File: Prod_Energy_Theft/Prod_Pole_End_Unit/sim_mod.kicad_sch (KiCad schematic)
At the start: 23 parts, among them J23 U.FL-R-SMT_01_, J28 JAE_SIM_Card_SF72S006, Q2 2N3904, U17 TXS0108EPW, U18 SIM7600G, U20 USBLC6-2SC6, U21 USBLC6-2SC6

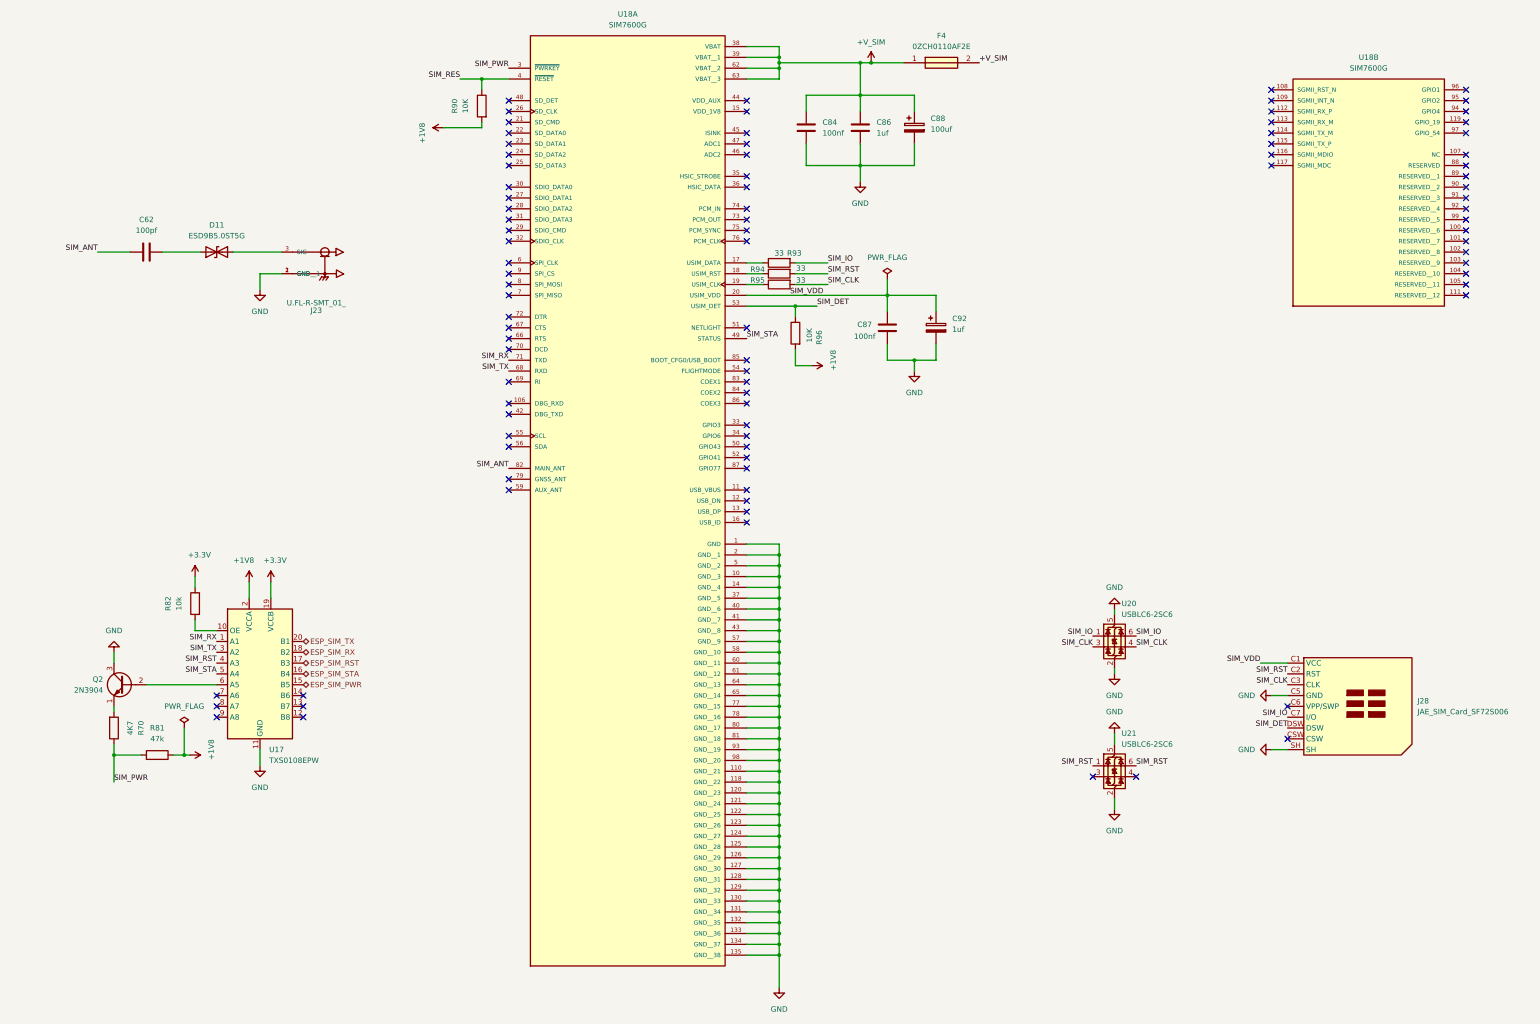
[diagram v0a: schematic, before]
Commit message: Chnages in power and ADE7816
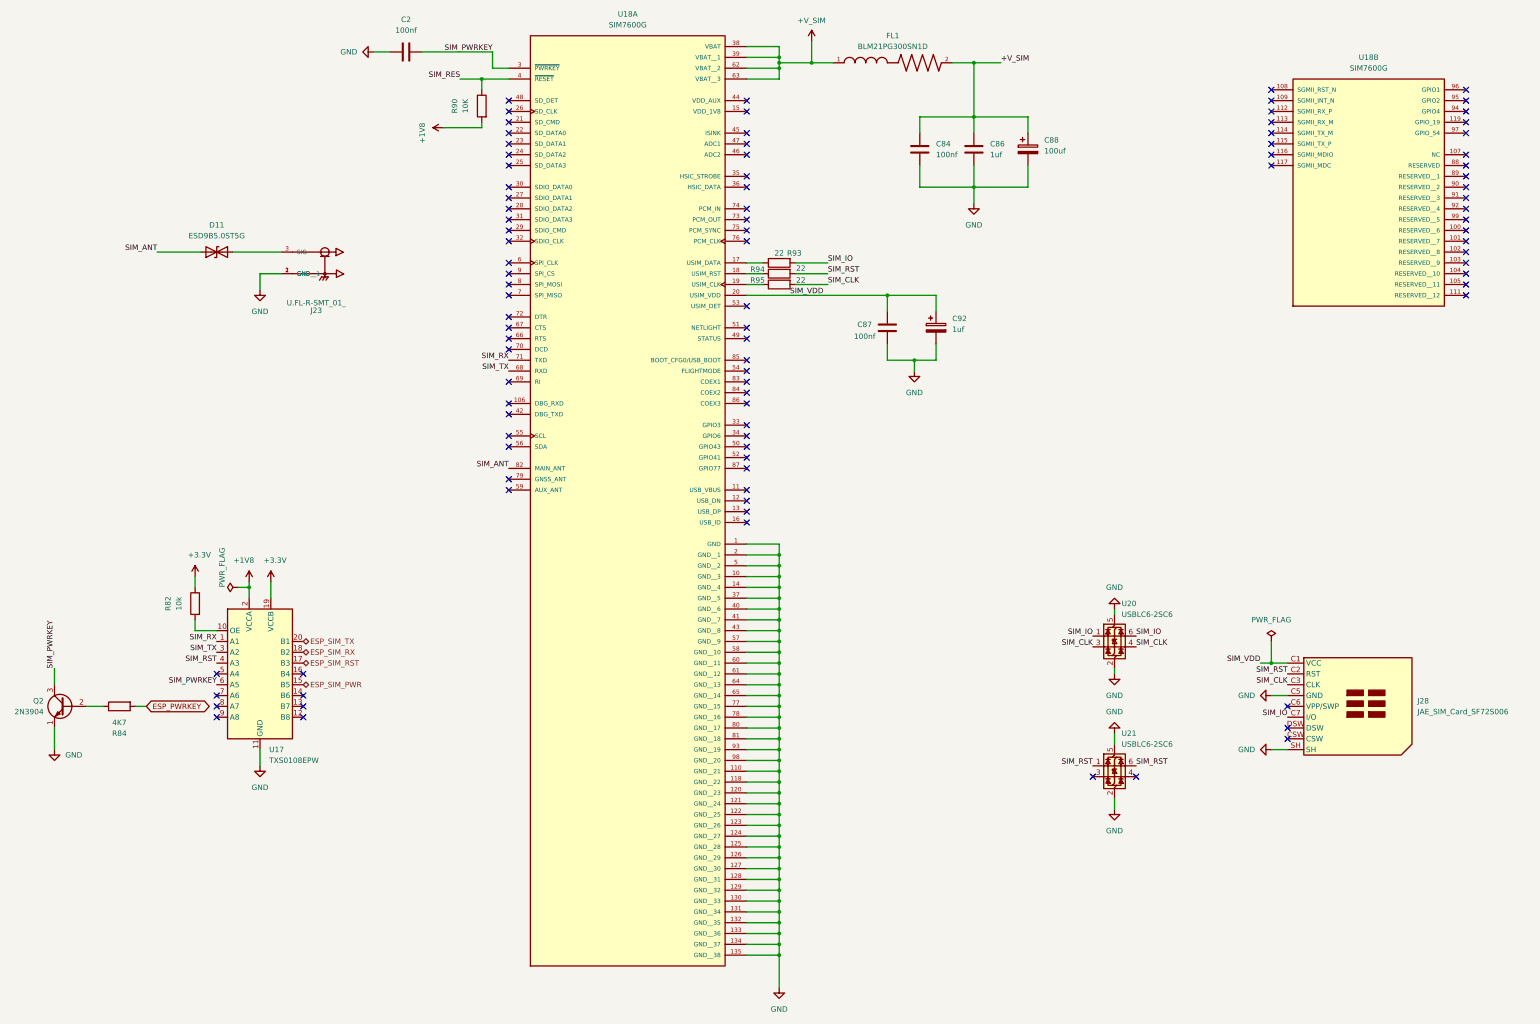
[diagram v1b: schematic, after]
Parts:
- removed C62: 100pf, Capacitor_SMD:C_0805_2012Metric, symbol Device:C
- removed F4: 0ZCH0110AF2E, Footprints.kicad_mod:FUSC3226X100N, symbol 0ZCH0110AF2E:0ZCH0110AF2E
- removed R70: 4K7, Resistor_SMD:R_0805_2012Metric, symbol Device:R
- removed R81: 47k, Resistor_SMD:R_0805_2012Metric, symbol Device:R
- removed R96: 10K, Resistor_SMD:R_0805_2012Metric, symbol Device:R
- added C2: 100nf, symbol Device:C
- added FL1: BLM21PG300SN1D, BLM21PG300SN1D:BEADC2012X105N, symbol BLM21PG300SN1D:BLM21PG300SN1D
- added R84: 4K7, Resistor_SMD:R_0805_2012Metric, symbol Device:R
- R93, R94, R95: value 33 -> 22
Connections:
- net +V_SIM: now also FL1.1, FL1.2
- net GND: now also Q2.1 (E), C2.1; no longer Q2.3 (C)
- net SIM_ANT: now also D11.1 (A1)
- net at Q2.2 (B): now also R84.1; no longer U17.6 (A5)
- net ESP_SIM_STA: no longer names the net of U17.16 (B4)
- net SIM_DET: no longer names the net of U18.53 (USIM_DET)
- net SIM_DET: no longer J28.DSW
- net SIM_PWR renamed SIM_PWRKEY
- net SIM_PWRKEY: now also Q2.3 (C), U17.6 (A5), C2.2
- net SIM_STA: no longer names the net of U17.5 (A4)
- net SIM_STA: no longer U18.49 (STATUS)
- new net ESP_PWRKEY: R84.2
- no-connect marks 91 -> 96
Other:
- moved on the sheet: C84, C86, C88, Q2

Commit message: PCB
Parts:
- C2: footprint (none) -> Capacitor_SMD:C_0805_2012Metric
- FL1: footprint BLM21PG300SN1D:BEADC2012X105N -> theftdetection:BEADC2012X105N
- J23: footprint U.FL-R-SMT_01_:HRS_U.FL-R-SMT_01_ -> theftdetection:HRS_U.FL-R-SMT_01_
- U18: footprint SIM7600G:IC_SIM7600G -> theftdetection:IC_SIM7600G
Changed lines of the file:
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@@
 	(wire
 		(pts
-			(xy 204.47 95.25) (xy 237.49 95.25)
-		)
-		(stroke
-			(width 0)
-			(type default)
-		)
-	)
-	(wire
-		(pts
 			(xy 212.09 194.31) (xy 212.09 196.85)
 		)
@@
 	(wire
 		(pts
+			(xy 204.47 95.25) (xy 237.49 95.25)
+		)
+		(stroke
+			(width 0)
+			(type default)
+		)
+	)
+	(wire
+		(pts
 			(xy 290.83 168.91) (xy 290.83 170.18)
 		)
@@
 			)
 		)
-		(property "Footprint" "SIM7600G:IC_SIM7600G"
+		(property "Footprint" "theftdetection:IC_SIM7600G"
 			(at 176.53 90.17 0)
 			(effects
@@
 			)
 		)
-		(property "Footprint" ""
+		(property "Footprint" "Capacitor_SMD:C_0805_2012Metric"
 			(at 128.27 37.1348 0)
 			(effects
@@
 			)
 		)
-		(property "Footprint" "SIM7600G:IC_SIM7600G"
+		(property "Footprint" "theftdetection:IC_SIM7600G"
 			(at 350.52 57.15 0)
 			(effects
@@
 			)
 		)
-		(property "Footprint" "BLM21PG300SN1D:BEADC2012X105N"
+		(property "Footprint" "theftdetection:BEADC2012X105N"
 			(at 240.03 40.64 0)
 			(effects
@@
 			)
 		)
-		(property "Footprint" "U.FL-R-SMT_01_:HRS_U.FL-R-SMT_01_"
+		(property "Footprint" "theftdetection:HRS_U.FL-R-SMT_01_"
 			(at 105.41 87.63 0)
 			(effects

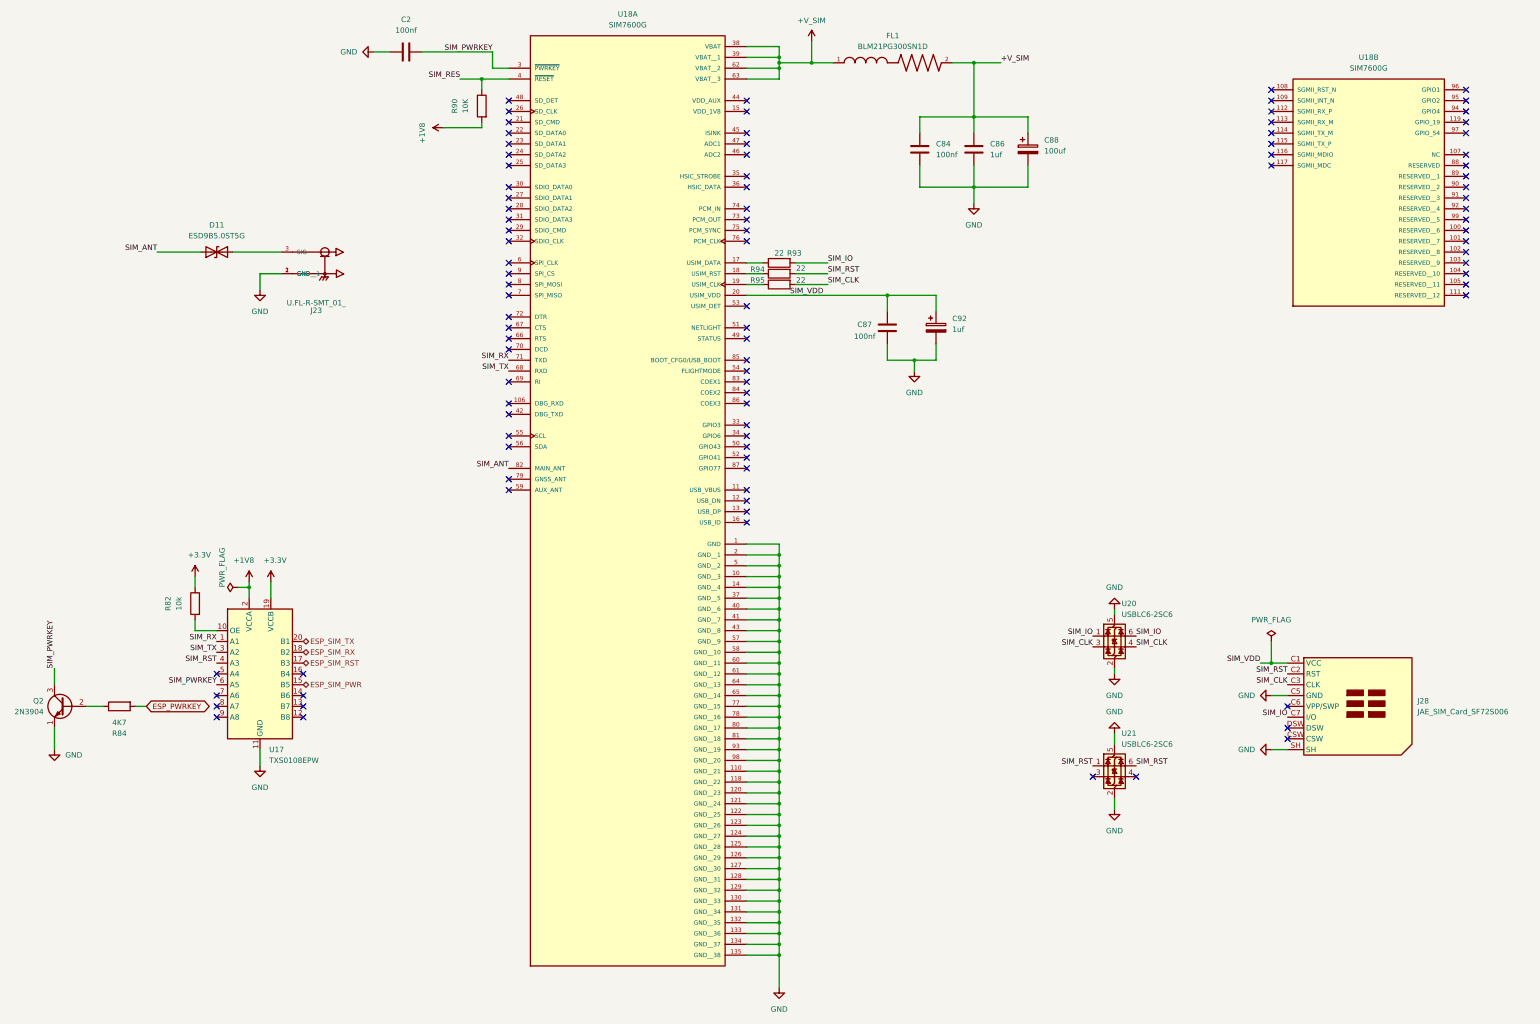
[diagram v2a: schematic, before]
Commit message: update in BOM list
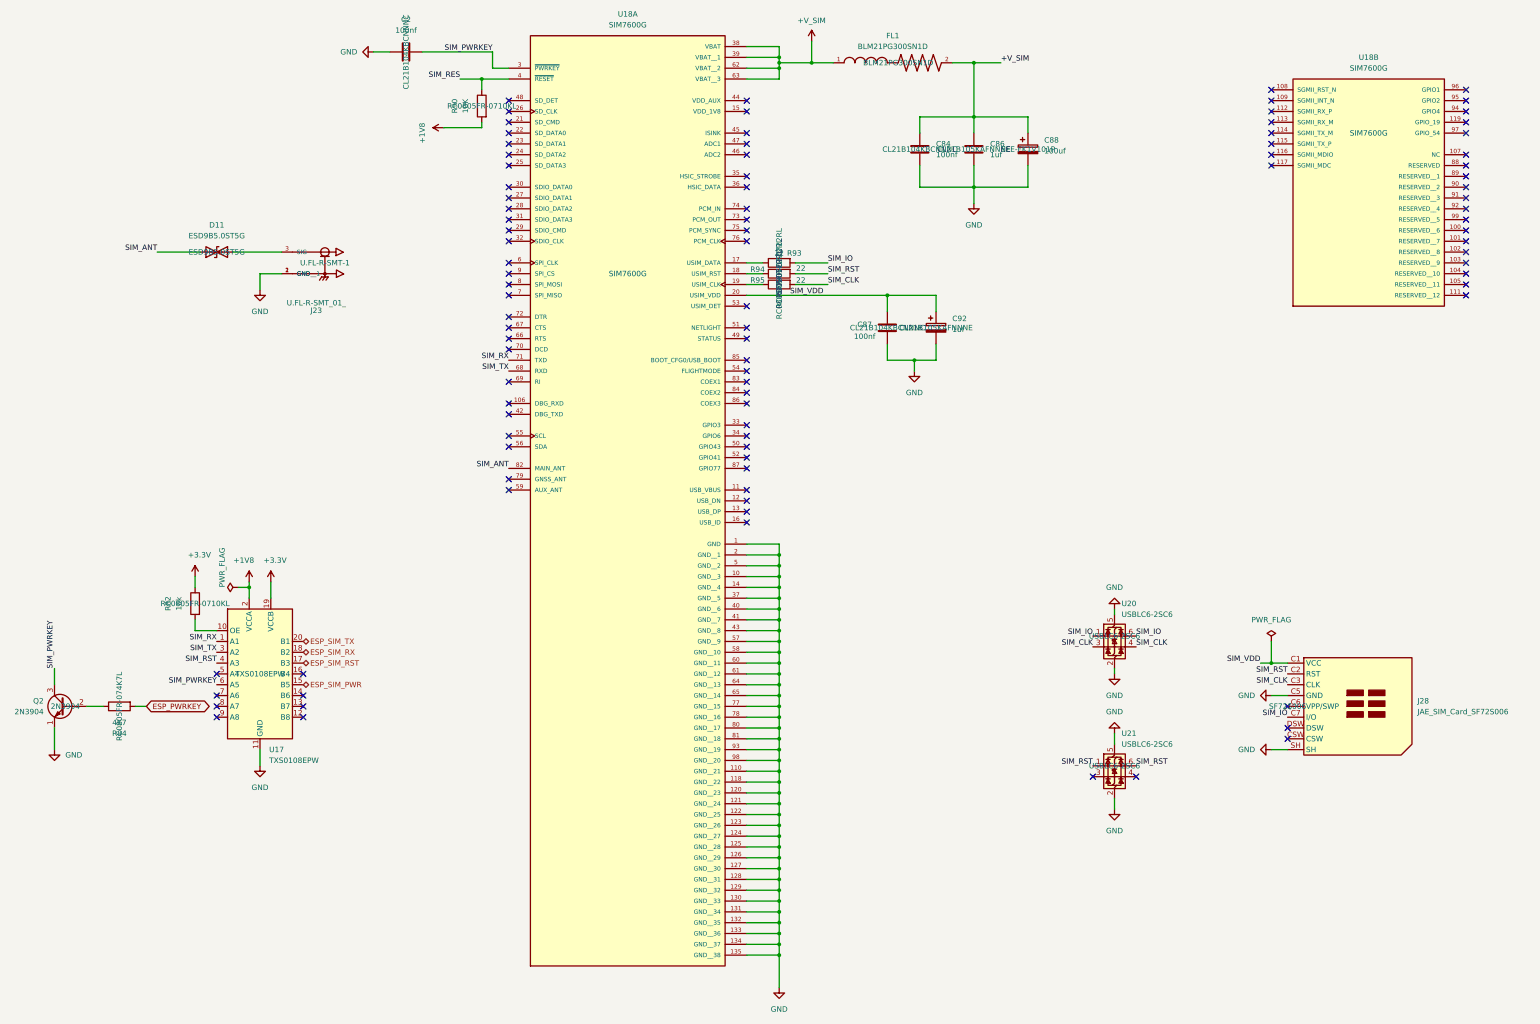
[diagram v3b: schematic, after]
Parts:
- C2, C84, C87: Part Number (none) -> CL21B104KBCNNNC
- C86, C92: Part Number (none) -> CL21B105KAFNNNE
- C88: Part Number (none) -> EEE-FK1V101P
- D11: Part Number (none) -> ESD9B5.0ST5G
- FL1: Part Number (none) -> BLM21PG300SN1D
- J23: Part Number (none) -> U.FL-R-SMT-1
- J28: Part Number (none) -> SF72S006
- Q2: Part Number (none) -> 2N3904
- R82, R90: Part Number (none) -> RC0805FR-0710KL
- R84: Part Number (none) -> RC0805FR-074K7L
- R93, R94, R95: Part Number (none) -> RC0805FR-0722RL
- U17: Part Number (none) -> TXS0108EPW
- U18: Part Number (none) -> SIM7600G
- U20, U21: Part Number (none) -> USBLC6-2SC6
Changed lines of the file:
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@@
 			)
 		)
+		(property "Part Number" "RC0805FR-0722RL "
+			(at 212.09 90.17 0)
+			(effects
+				(font
+					(size 1.27 1.27)
+				)
+			)
+		)
 		(pin "1"
 		)
@@
 			)
 		)
+		(property "Part Number" "RC0805FR-0710KL "
+			(at 74.93 167.64 0)
+			(effects
+				(font
+					(size 1.27 1.27)
+				)
+			)
+		)
 		(pin "1"
 		)
@@
 			)
 		)
+		(property "Part Number" "TXS0108EPW "
+			(at 90.17 184.15 0)
+			(effects
+				(font
+					(size 1.27 1.27)
+				)
+			)
+		)
 		(pin "19"
 		)
@@
 			)
 		)
+		(property "Part Number" "RC0805FR-0722RL "
+			(at 212.09 87.63 0)
+			(effects
+				(font
+					(size 1.27 1.27)
+				)
+			)
+		)
 		(pin "1"
 		)
@@
 			)
 		)
+		(property "Part Number" "SIM7600G "
+			(at 176.53 90.17 0)
+			(effects
+				(font
+					(size 1.27 1.27)
+				)
+			)
+		)
 		(pin "98"
 		)
@@
 			)
 		)
+		(property "Part Number" "SF72S006 "
+			(at 331.47 191.77 0)
+			(effects
+				(font
+					(size 1.27 1.27)
+				)
+			)
+		)
 		(pin "C1"
 		)
@@
 			)
 		)
+		(property "Part Number" "CL21B105KAFNNNE "
+			(at 248.92 102.87 0)
+			(effects
+				(font
+					(size 1.27 1.27)
+				)
+			)
+		)
 		(pin "1"
 		)
@@
 			)
 		)
+		(property "Part Number" "RC0805FR-074K7L "
+			(at 57.15 191.77 0)
+			(effects
+				(font
+					(size 1.27 1.27)
+				)
+			)
+		)
 		(pin "1"
 		)
@@
 			)
 		)
+		(property "Part Number" "ESD9B5.0ST5G "
+			(at 80.01 85.09 0)
+			(effects
+				(font
+					(size 1.27 1.27)
+				)
+			)
+		)
 		(pin "1"
 		)
@@
 			)
 		)
+		(property "Part Number" "USBLC6-2SC6 "
+			(at 290.83 175.26 0)
+			(effects
+				(font
+					(size 1.27 1.27)
+				)
+			)
+		)
 		(pin "1"
 		)
@@
 			)
 		)
+		(property "Part Number" "RC0805FR-0710KL "
+			(at 142.24 50.8 0)
+			(effects
+				(font
+					(size 1.27 1.27)
+				)
+			)
+		)
 		(pin "1"
 		)
@@
 			)
 		)
+		(property "Part Number" "CL21B104KBCNNNC "
+			(at 124.46 38.1 0)
+			(effects
+				(font
+					(size 1.27 1.27)
+				)
+			)
+		)
 		(pin "2"
 		)
@@
 			)
 		)
+		(property "Part Number" "SIM7600G "
+			(at 350.52 57.15 0)
+			(effects
+				(font
+					(size 1.27 1.27)
+				)
+			)
+		)
 		(pin "98"
 		)
@@
 			)
 		)
+		(property "Part Number" "EEE-FK1V101P "
+			(at 270.51 60.96 0)
+			(effects
+				(font
+					(size 1.27 1.27)
+				)
+			)
+		)
 		(pin "1"
 		)
@@
 			)
 		)
+		(property "Part Number" "RC0805FR-0722RL "
+			(at 212.09 92.71 0)
+			(effects
+				(font
+					(size 1.27 1.27)
+				)
+			)
+		)
 		(pin "1"
 		)
@@
 			)
 		)
+		(property "Part Number" "BLM21PG300SN1D "
+			(at 240.03 40.64 0)
+			(effects
+				(font
+					(size 1.27 1.27)
+				)
+			)
+		)
 		(pin "1"
 		)
@@
 			)
 		)
+		(property "Part Number" "U.FL-R-SMT-1 "
+			(at 105.41 87.63 0)
+			(effects
+				(font
+					(size 1.27 1.27)
+				)
+			)
+		)
 		(pin "2"
 		)
@@
 			)
 		)
+		(property "Part Number" "CL21B104KBCNNNC "
+			(at 245.11 60.96 0)
+			(effects
+				(font
+					(size 1.27 1.27)
+				)
+			)
+		)
 		(pin "1"
 		)
@@
 			)
 		)
+		(property "Part Number" "2N3904 "
+			(at 44.45 191.77 0)
+			(effects
+				(font
+					(size 1.27 1.27)
+				)
+			)
+		)
 		(pin "3"
 		)
@@
 			)
 		)
+		(property "Part Number" "USBLC6-2SC6 "
+			(at 290.83 205.74 0)
+			(effects
+				(font
+					(size 1.27 1.27)
+				)
+			)
+		)
 		(pin "1"
 		)
@@
 			)
 		)
+		(property "Part Number" "CL21B104KBCNNNC "
+			(at 237.49 102.87 0)
+			(effects
+				(font
+					(size 1.27 1.27)
+				)
+			)
+		)
 		(pin "1"
 		)
@@
 			)
 		)
+		(property "Part Number" "CL21B105KAFNNNE "
+			(at 257.81 60.96 0)
+			(effects
+				(font
+					(size 1.27 1.27)
+				)
+			)
+		)
